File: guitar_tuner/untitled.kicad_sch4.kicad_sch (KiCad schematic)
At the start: 9 parts

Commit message: FootprintUpdate
Upodate to Footprints
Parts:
- C15, C16, C17, C18, C19, C20, C21, C22: footprint (none) -> Capacitor_SMD:C_0805_2012Metric_Pad1.18x1.45mm_HandSolder
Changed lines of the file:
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@@
 			)
 		)
-		(property "Footprint" ""
+		(property "Footprint" "Capacitor_SMD:C_0805_2012Metric_Pad1.18x1.45mm_HandSolder"
 			(at 196.85 99.06 0)
 			(effects
@@
 			)
 		)
-		(property "Footprint" ""
+		(property "Footprint" "Capacitor_SMD:C_0805_2012Metric_Pad1.18x1.45mm_HandSolder"
 			(at 200.66 116.84 0)
 			(effects
@@
 			)
 		)
-		(property "Footprint" ""
+		(property "Footprint" "Capacitor_SMD:C_0805_2012Metric_Pad1.18x1.45mm_HandSolder"
 			(at 191.77 96.52 0)
 			(effects
@@
 			)
 		)
-		(property "Footprint" ""
+		(property "Footprint" "Capacitor_SMD:C_0805_2012Metric_Pad1.18x1.45mm_HandSolder"
 			(at 201.93 101.6 0)
 			(effects
@@
 			)
 		)
-		(property "Footprint" ""
+		(property "Footprint" "Capacitor_SMD:C_0805_2012Metric_Pad1.18x1.45mm_HandSolder"
 			(at 185.42 116.84 0)
 			(effects
@@
 			)
 		)
-		(property "Footprint" ""
+		(property "Footprint" "Capacitor_SMD:C_0805_2012Metric_Pad1.18x1.45mm_HandSolder"
 			(at 186.69 93.98 0)
 			(effects
@@
 			)
 		)
-		(property "Footprint" ""
+		(property "Footprint" "Capacitor_SMD:C_0805_2012Metric_Pad1.18x1.45mm_HandSolder"
 			(at 185.42 111.76 0)
 			(effects
@@
 			)
 		)
-		(property "Footprint" ""
+		(property "Footprint" "Capacitor_SMD:C_0805_2012Metric_Pad1.18x1.45mm_HandSolder"
 			(at 182.88 91.44 0)
 			(effects

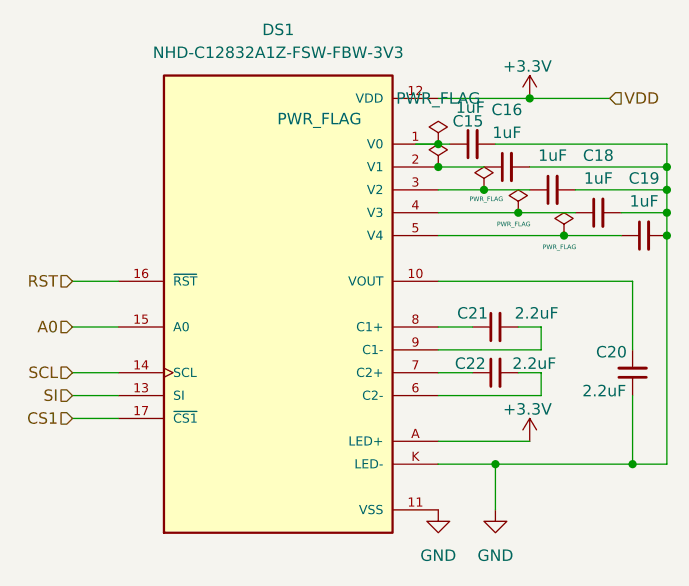
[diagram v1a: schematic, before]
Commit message: ERC Check
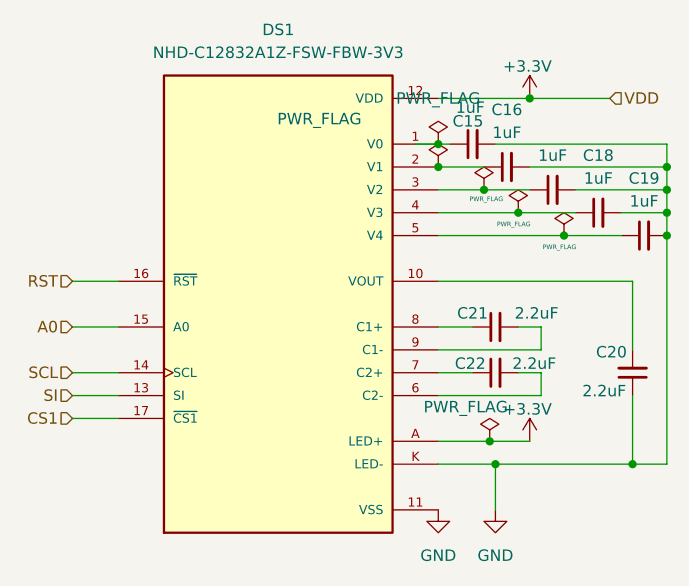
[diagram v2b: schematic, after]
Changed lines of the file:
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@@
+	)
+	(junction
+		(at 184.785 124.46)
+		(diameter 0)
+		(color 0 0 0 0)
 	)
 	(junction
@@
 	(wire
 		(pts
-			(xy 179.07 124.46) (xy 189.23 124.46)
+			(xy 179.07 124.46) (xy 184.785 124.46)
 		)
 		(stroke
@@
 		(pts
 			(xy 179.07 119.38) (xy 190.5 119.38)
+		)
+		(stroke
+			(width 0)
+			(type default)
+		)
+	)
+	(wire
+		(pts
+			(xy 184.785 124.46) (xy 189.23 124.46)
 		)
 		(stroke
@@
 					(unit 1)
 				)
+			)
+		)
+	)
+	(symbol
+		(lib_id "power:PWR_FLAG")
+		(at 184.785 124.46 0)
+		(unit 1)
+		(exclude_from_sim no)
+		(in_bom yes)
+		(on_board yes)
+		(dnp no)
+		(property "Reference" "#FLG08"
+			(at 184.785 122.555 0)
+			(effects
+				(font
+					(size 1.27 1.27)
+				)
+				(hide yes)
+			)
+		)
+		(property "Value" "PWR_FLAG"
+			(at 182.118 120.65 0)
+			(effects
+				(font
+					(size 1.27 1.27)
+				)
+			)
+		)
+		(property "Footprint" ""
+			(at 184.785 124.46 0)
+			(effects
+				(font
+					(size 1.27 1.27)
+				)
+				(hide yes)
+			)
+		)
+		(property "Datasheet" "~"
+			(at 184.785 124.46 0)
+			(effects
+				(font
+					(size 1.27 1.27)
+				)
+				(hide yes)
+			)
+		)
+		(property "Description" "Special symbol for telling ERC where power comes from"
+			(at 184.785 124.46 0)
+			(effects
+				(font
+					(size 1.27 1.27)
+				)
+				(hide yes)
+			)
+		)
+		(pin "1"
+		)
+		(instances
+			(project "guitar_tuner"
+				(path "/66cd80e7-aa2b-4408-b572-7f7169004942/45fd4d01-e263-4e5a-af0b-cb18a369c171"
+					(reference "#FLG08")
+					(unit 1)
+				)

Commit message: Footprint Fix
I hope
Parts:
- DS1: footprint NHD-C12832A1Z-FSW-FBW-3V3:LCD_NHD-C12832A1Z-FSW-FBW-3V3 -> LCD_NUD-C12832A1Z:LCD_NHD-C12832A1Z-FSW-FBW-3V3
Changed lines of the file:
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@@
 			)
 		)
-		(property "Footprint" "NHD-C12832A1Z-FSW-FBW-3V3:LCD_NHD-C12832A1Z-FSW-FBW-3V3"
+		(property "Footprint" "LCD_NUD-C12832A1Z:LCD_NHD-C12832A1Z-FSW-FBW-3V3"
 			(at 161.29 109.22 0)
 			(effects
